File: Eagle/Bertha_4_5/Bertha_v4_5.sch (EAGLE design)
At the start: 132 parts, among them CON1 JACK_DC_BARREL, CON2 JACK_DC_BARREL, IC1 MCP1703DB, IC4 DRV8811, J1 RJ12RIGHTANGLE-I2C, J2 RJ12RIGHTANGLE-I2C, Q5 BSP75, Q6 BSP75, U1 HX711, U100 RN2483, X1 1503_09, X2 8MHz, X3 FH12-08S-1SH, X4 MINI-USB

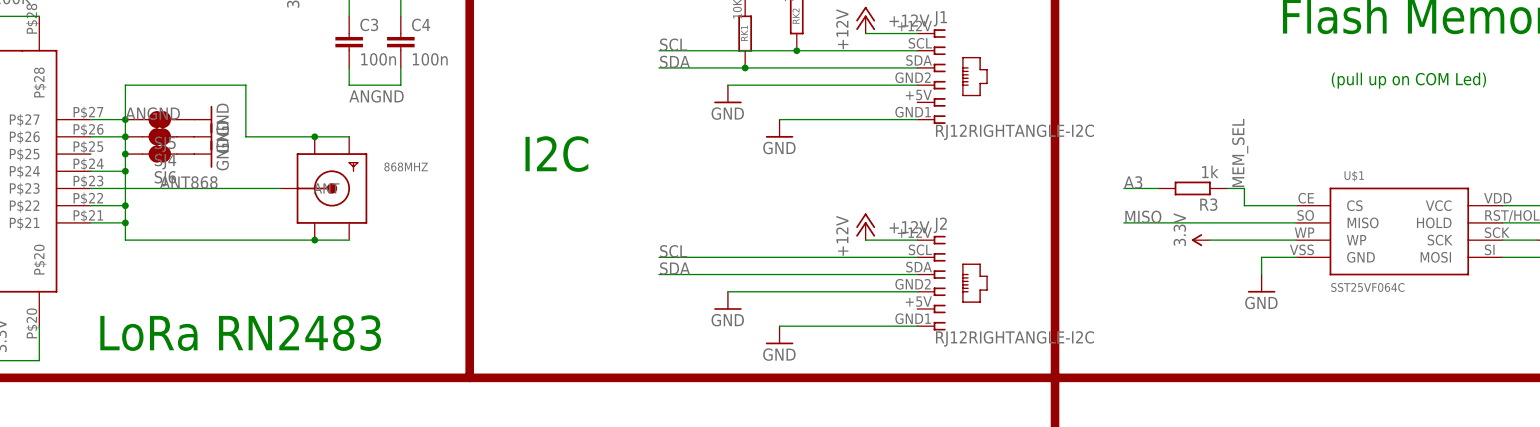
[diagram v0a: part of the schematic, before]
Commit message: LoRa Antenna moved inward, rerouted more simply the SST Flash memory closes #85 closes #86 closes #87, need to regen Gerbers
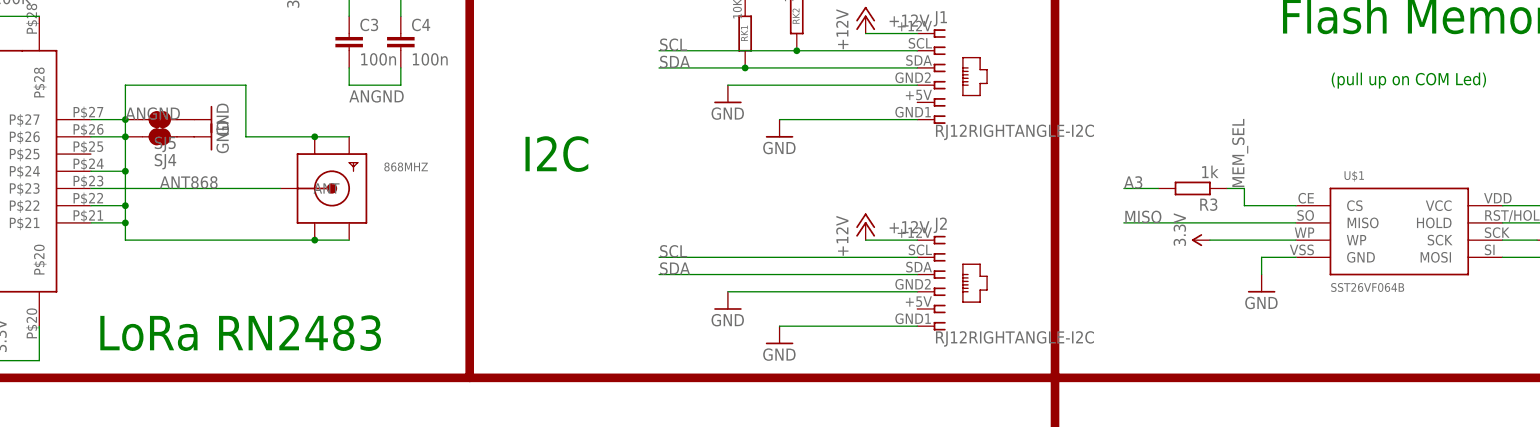
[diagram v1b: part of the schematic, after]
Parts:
- removed SJ6: JUMPER-PAD-2-NC_BY_TRACE, SparkFun-Passives:JUMPER-PAD-2-NC_BY_TRACE
- U$1: value SST25VF064C -> SST26VF064B
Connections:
- net ANGND: no longer SJ6.2
- net GND: no longer SJ6.1
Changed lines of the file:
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@@
 <part name="RUSB1" library="resistor" deviceset="R-EU_" device="M0805" value="22"/>
 <part name="CU9" library="rcl" deviceset="C-EU" device="C0805" value="10uF"/>
-<part name="U$1" library="BertaLib" deviceset="SST25VF064C" device=""/>
+<part name="U$1" library="BertaLib" deviceset="SST25VF064C" device="" value="SST26VF064B"/>
 <part name="RK2" library="resistor" deviceset="R-EU_" device="M0805" value="10K"/>
 <part name="RK1" library="resistor" deviceset="R-EU_" device="M0805" value="10K"/>
@@
 <part name="SJ5" library="SparkFun-Passives" deviceset="JUMPER-PAD-2-NC_BY_TRACE" device="" value=""/>
 <part name="GND16" library="SparkFun-Aesthetics" deviceset="GND" device=""/>
-<part name="SJ6" library="SparkFun-Passives" deviceset="JUMPER-PAD-2-NC_BY_TRACE" device="" value=""/>
-<part name="GND22" library="SparkFun-Aesthetics" deviceset="GND" device=""/>
 <part name="100K" library="rcl" deviceset="R-EU_" device="R0805" value="100k"/>
 <part name="GND" library="Headerlibrary" deviceset="PINHD-1X1" device="" value="GND"/>
@@
 <instance part="SJ5" gate="G$1" x="254" y="264.16" rot="R180"/>
 <instance part="GND16" gate="1" x="261.62" y="264.16" rot="R90"/>
-<instance part="SJ6" gate="G$1" x="254" y="259.08" rot="R180"/>
-<instance part="GND22" gate="1" x="261.62" y="259.08" rot="R90"/>
 <instance part="100K" gate="G$1" x="231.14" y="284.48" rot="R180"/>
 <instance part="GND" gate="G$1" x="459.74" y="88.9"/>
@@
 </segment>
 <segment>
-<pinref part="SJ6" gate="G$1" pin="1"/>
-<pinref part="GND22" gate="1" pin="GND"/>
-</segment>
-<segment>
 <pinref part="GND" gate="G$1" pin="1"/>
 <pinref part="GND28" gate="1" pin="GND"/>
@@
 <pinref part="U100" gate="G$1" pin="P$26"/>
 <wire x1="248.92" y1="261.62" x2="243.84" y2="261.62" width="0.1524" layer="91"/>
-<wire x1="248.92" y1="261.62" x2="248.92" y2="259.08" width="0.1524" layer="91"/>
 <junction x="248.92" y="261.62"/>
 <pinref part="U100" gate="G$1" pin="P$24"/>
-<wire x1="248.92" y1="259.08" x2="248.92" y2="256.54" width="0.1524" layer="91"/>
+<wire x1="248.92" y1="261.62" x2="248.92" y2="256.54" width="0.1524" layer="91"/>
 <wire x1="248.92" y1="256.54" x2="243.84" y2="256.54" width="0.1524" layer="91"/>
 <wire x1="248.92" y1="256.54" x2="248.92" y2="251.46" width="0.1524" layer="91"/>
@@
 <pinref part="SJ5" gate="G$1" pin="2"/>
 <junction x="248.92" y="264.16"/>
-<pinref part="SJ6" gate="G$1" pin="2"/>
-<junction x="248.92" y="259.08"/>
 <pinref part="868MHZ" gate="G$1" pin="GND4"/>
 <pinref part="868MHZ" gate="G$1" pin="GND3"/>

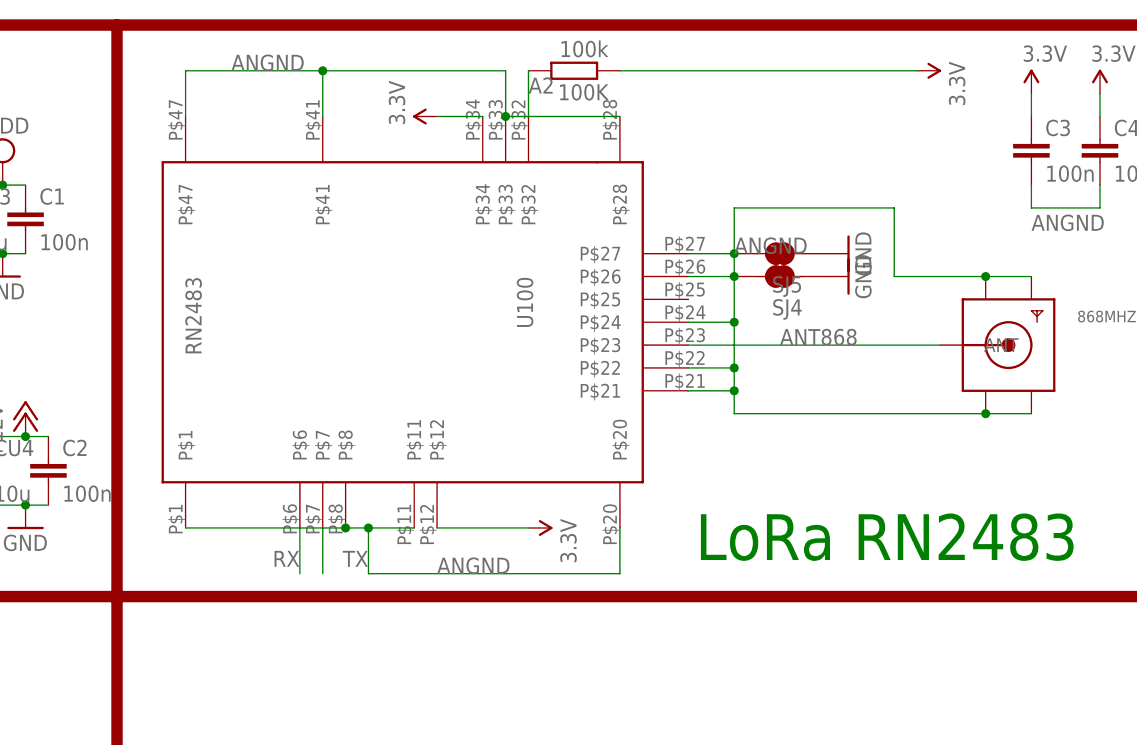
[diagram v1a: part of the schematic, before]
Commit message: Modified LoRa footprint for ease of soldering Still need to regen Gerbers
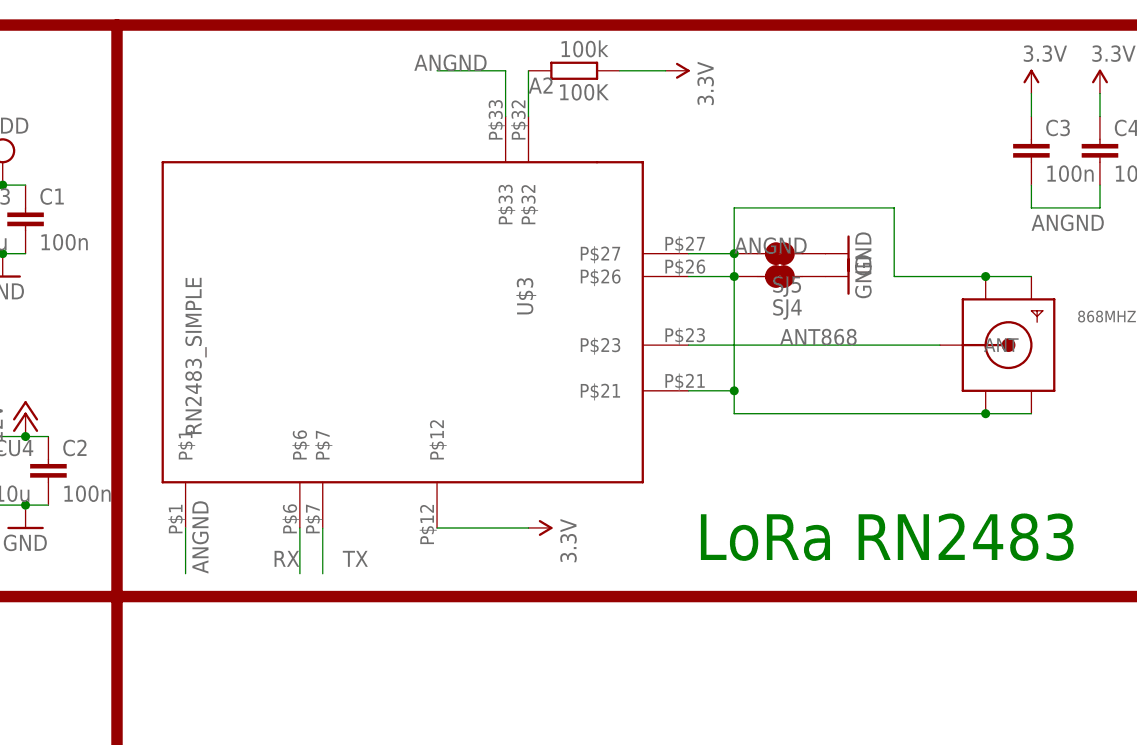
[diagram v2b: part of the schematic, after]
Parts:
- removed U100: RN2483, Octanis1:RN2483
- added U$3: RN2483_SIMPLE, Octanis1_bioreactorPort:RN2483_SIMPLE
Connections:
- net 3.3V: now also U$3.P$12; no longer U100.P$12, U100.P$34
- net A2: now also U$3.P$32; no longer U100.P$32
- net ANGND: now also U$3.P$1, U$3.P$21, U$3.P$26, U$3.P$27, U$3.P$33; no longer U100.P$1, U100.P$11, U100.P$20, U100.P$21, U100.P$22, U100.P$24, U100.P$26, U100.P$27, U100.P$28, U100.P$33, U100.P$41, U100.P$47, U100.P$8
- net ANT868: now also U$3.P$23; no longer U100.P$23
- net RX: now also U$3.P$6; no longer U100.P$6
- net TX: now also U$3.P$7; no longer U100.P$7
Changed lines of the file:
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@@
 <?xml version="1.0" encoding="utf-8"?>
 <!DOCTYPE eagle SYSTEM "eagle.dtd">
-<eagle version="7.5.0">
+<eagle version="8.0.1">
 <drawing>
 <settings>
@@
 <part name="SJ1" library="jumper" deviceset="SJ" device=""/>
 <part name="SJ3" library="jumper" deviceset="SJ" device=""/>
-<part name="U100" library="Octanis1" deviceset="RN2483" device="" value="RN2483"/>
 <part name="GND32" library="supply1" deviceset="GND" device=""/>
 <part name="GND38" library="supply1" deviceset="GND" device=""/>
@@
 <part name="P+10" library="supply1" deviceset="+12V" device=""/>
 <part name="P+11" library="supply1" deviceset="+12V" device=""/>
-<part name="P+17" library="SparkFun" deviceset="3.3V" device=""/>
 <part name="P+19" library="SparkFun" deviceset="3.3V" device=""/>
 <part name="P+22" library="SparkFun" deviceset="3.3V" device=""/>
@@
 <part name="JP3" library="jumper" deviceset="JP4E" device=""/>
 <part name="R4" library="rcl" deviceset="R-EU_" device="R0805" value="100"/>
+<part name="U$3" library="Octanis1_bioreactorPort" deviceset="RN2483_SIMPLE" device=""/>
 </parts>
 <sheets>
@@
 <instance part="SJ1" gate="1" x="393.7" y="170.18" rot="R90"/>
 <instance part="SJ3" gate="1" x="142.24" y="149.86" rot="R270"/>
-<instance part="U100" gate="G$1" x="210.82" y="256.54" rot="R270"/>
 <instance part="GND32" gate="1" x="398.78" y="154.94" rot="R270"/>
 <instance part="GND38" gate="1" x="398.78" y="139.7" rot="R270"/>
@@
 <instance part="P+10" gate="1" x="358.14" y="248.92"/>
 <instance part="P+11" gate="1" x="358.14" y="279.4"/>
-<instance part="P+17" gate="G$1" x="215.9" y="279.4" rot="R90"/>
 <instance part="P+19" gate="G$1" x="281.94" y="281.94"/>
-<instance part="P+22" gate="G$1" x="269.24" y="284.48" rot="R270"/>
+<instance part="P+22" gate="G$1" x="241.3" y="284.48" rot="R270"/>
 <instance part="P+25" gate="G$1" x="289.56" y="281.94"/>
 <instance part="P+26" gate="G$1" x="226.06" y="233.68" rot="R270"/>
@@
 <instance part="JP3" gate="G$1" x="350.52" y="127" rot="R270"/>
 <instance part="R4" gate="G$1" x="279.4" y="53.34" rot="MR90"/>
+<instance part="U$3" gate="G$1" x="210.82" y="256.54" rot="R270"/>
 </instances>
 <busses>
@@
 <segment>
 <pinref part="100K" gate="G$1" pin="2"/>
-<pinref part="U100" gate="G$1" pin="P$32"/>
 <wire x1="226.06" y1="284.48" x2="226.06" y2="279.4" width="0.1524" layer="91"/>
 <label x="226.06" y="281.94" size="1.778" layer="95"/>
+<pinref part="U$3" gate="G$1" pin="P$32"/>
 </segment>
 </net>
@@
 </segment>
 <segment>
-<wire x1="215.9" y1="279.4" x2="220.98" y2="279.4" width="0.1524" layer="91"/>
-<pinref part="U100" gate="G$1" pin="P$34"/>
-<pinref part="P+17" gate="G$1" pin="3.3V"/>
-</segment>
-<segment>
 <wire x1="281.94" y1="281.94" x2="281.94" y2="279.4" width="0.1524" layer="91"/>
 <pinref part="C3" gate="G$1" pin="1"/>
@@
 </segment>
 <segment>
-<wire x1="236.22" y1="284.48" x2="269.24" y2="284.48" width="0.1524" layer="91"/>
+<wire x1="236.22" y1="284.48" x2="241.3" y2="284.48" width="0.1524" layer="91"/>
 <pinref part="P+22" gate="G$1" pin="3.3V"/>
 <pinref part="100K" gate="G$1" pin="1"/>
@@
 <segment>
 <wire x1="226.06" y1="233.68" x2="215.9" y2="233.68" width="0.1524" layer="91"/>
-<pinref part="U100" gate="G$1" pin="P$12"/>
 <pinref part="P+26" gate="G$1" pin="3.3V"/>
+<pinref part="U$3" gate="G$1" pin="P$12"/>
 </segment>
 <segment>
@@
 </segment>
 <segment>
-<pinref part="U100" gate="G$1" pin="P$7"/>
 <wire x1="203.2" y1="233.68" x2="203.2" y2="228.6" width="0.1524" layer="91"/>
 <label x="208.28" y="231.14" size="1.778" layer="95" rot="R180"/>
+<pinref part="U$3" gate="G$1" pin="P$7"/>
 </segment>
 </net>
@@
 </segment>
 <segment>
-<pinref part="U100" gate="G$1" pin="P$6"/>
 <wire x1="200.66" y1="233.68" x2="200.66" y2="228.6" width="0.1524" layer="91"/>
 <label x="200.66" y="231.14" size="1.778" layer="95" rot="R180"/>
+<pinref part="U$3" gate="G$1" pin="P$6"/>
 </segment>
 </net>
@@
 <net name="ANT868" class="0">
 <segment>
-<pinref part="U100" gate="G$1" pin="P$23"/>
 <wire x1="271.78" y1="254" x2="243.84" y2="254" width="0.1524" layer="91"/>
 <label x="254" y="254" size="1.778" layer="95"/>
 <pinref part="868MHZ" gate="G$1" pin="ANT"/>
+<pinref part="U$3" gate="G$1" pin="P$23"/>
 </segment>
 </net>
@@
 <net name="ANGND" class="0">
 <segment>
-<pinref part="U100" gate="G$1" pin="P$1"/>
-<pinref part="U100" gate="G$1" pin="P$8"/>
-<wire x1="187.96" y1="233.68" x2="205.74" y2="233.68" width="0.1524" layer="91"/>
-<pinref part="U100" gate="G$1" pin="P$11"/>
-<wire x1="205.74" y1="233.68" x2="208.28" y2="233.68" width="0.1524" layer="91"/>
-<junction x="205.74" y="233.68"/>
-<pinref part="U100" gate="G$1" pin="P$20"/>
-<wire x1="208.28" y1="233.68" x2="213.36" y2="233.68" width="0.1524" layer="91"/>
-<wire x1="236.22" y1="233.68" x2="236.22" y2="228.6" width="0.1524" layer="91"/>
-<wire x1="236.22" y1="228.6" x2="208.28" y2="228.6" width="0.1524" layer="91"/>
-<wire x1="208.28" y1="228.6" x2="208.28" y2="233.68" width="0.1524" layer="91"/>
-<junction x="208.28" y="233.68"/>
-<label x="215.9" y="228.6" size="1.778" layer="95"/>
+<wire x1="187.96" y1="233.68" x2="187.96" y2="228.6" width="0.1524" layer="91"/>
+<label x="190.5" y="228.6" size="1.778" layer="95" rot="R90"/>
+<pinref part="U$3" gate="G$1" pin="P$1"/>
 </segment>
 <segment>
-<pinref part="U100" gate="G$1" pin="P$33"/>
 <wire x1="223.52" y1="279.4" x2="223.52" y2="284.48" width="0.1524" layer="91"/>
-<pinref part="U100" gate="G$1" pin="P$41"/>
-<wire x1="223.52" y1="284.48" x2="203.2" y2="284.48" width="0.1524" layer="91"/>
-<wire x1="203.2" y1="284.48" x2="203.2" y2="279.4" width="0.1524" layer="91"/>
-<pinref part="U100" gate="G$1" pin="P$47"/>
-<wire x1="203.2" y1="284.48" x2="187.96" y2="284.48" width="0.1524" layer="91"/>
-<wire x1="187.96" y1="284.48" x2="187.96" y2="279.4" width="0.1524" layer="91"/>
-<junction x="203.2" y="284.48"/>
-<label x="193.04" y="284.48" size="1.778" layer="95"/>
-<pinref part="U100" gate="G$1" pin="P$28"/>
-<wire x1="223.52" y1="279.4" x2="236.22" y2="279.4" width="0.1524" layer="91"/>
-<junction x="223.52" y="279.4"/>
+<wire x1="223.52" y1="284.48" x2="215.9" y2="284.48" width="0.1524" layer="91"/>
+<label x="213.36" y="284.48" size="1.778" layer="95"/>
+<pinref part="U$3" gate="G$1" pin="P$33"/>
 </segment>
 <segment>
-<pinref part="U100" gate="G$1" pin="P$27"/>
 <wire x1="243.84" y1="264.16" x2="248.92" y2="264.16" width="0.1524" layer="91"/>
 <wire x1="248.92" y1="264.16" x2="248.92" y2="261.62" width="0.1524" layer="91"/>
-<pinref part="U100" gate="G$1" pin="P$26"/>
 <wire x1="248.92" y1="261.62" x2="243.84" y2="261.62" width="0.1524" layer="91"/>
 <junction x="248.92" y="261.62"/>
-<pinref part="U100" gate="G$1" pin="P$24"/>
-<wire x1="248.92" y1="261.62" x2="248.92" y2="256.54" width="0.1524" layer="91"/>
-<wire x1="248.92" y1="256.54" x2="243.84" y2="256.54" width="0.1524" layer="91"/>
-<wire x1="248.92" y1="256.54" x2="248.92" y2="251.46" width="0.1524" layer="91"/>
-<junction x="248.92" y="256.54"/>
-<pinref part="U100" gate="G$1" pin="P$22"/>
-<wire x1="248.92" y1="251.46" x2="243.84" y2="251.46" width="0.1524" layer="91"/>
-<pinref part="U100" gate="G$1" pin="P$21"/>
+<wire x1="248.92" y1="261.62" x2="248.92" y2="248.92" width="0.1524" layer="91"/>
 <wire x1="243.84" y1="248.92" x2="248.92" y2="248.92" width="0.1524" layer="91"/>
-<wire x1="248.92" y1="248.92" x2="248.92" y2="251.46" width="0.1524" layer="91"/>
-<junction x="248.92" y="251.46"/>
 <label x="248.92" y="264.16" size="1.778" layer="95"/>
 <pinref part="SJ4" gate="G$1" pin="2"/>
@@
 <wire x1="266.7" y1="269.24" x2="248.92" y2="269.24" width="0.1524" layer="91"/>
 <wire x1="248.92" y1="269.24" x2="248.92" y2="264.16" width="0.1524" layer="91"/>
+<pinref part="U$3" gate="G$1" pin="P$21"/>
+<pinref part="U$3" gate="G$1" pin="P$26"/>
+<pinref part="U$3" gate="G$1" pin="P$27"/>
 </segment>
 <segment>
